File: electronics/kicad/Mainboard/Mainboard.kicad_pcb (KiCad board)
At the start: 2 copper layers, 99 x 53 mm, 32 parts, among them J1 MCU Power, J10 Box Button 1, J11 Box Button 2, J12 Conn_01x05, J13 Extra Button, J2 Conn_01x05, J3 Conn_01x05, J4 Conn_01x05, J5 Conn_01x05, J6 Conn_01x05, J7 X-Axis Hall, J8 Y-Axis Hall, J9 USB_A_Stacked, M2 MountingHole_2.7mm_M2.5_DIN96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, M2.5 MountingHole_2.7mm_M2.5_DIN96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, U1 ESP32-C6-DevKitC-1, U2 MCP23017_SP, U3 SP3485CP

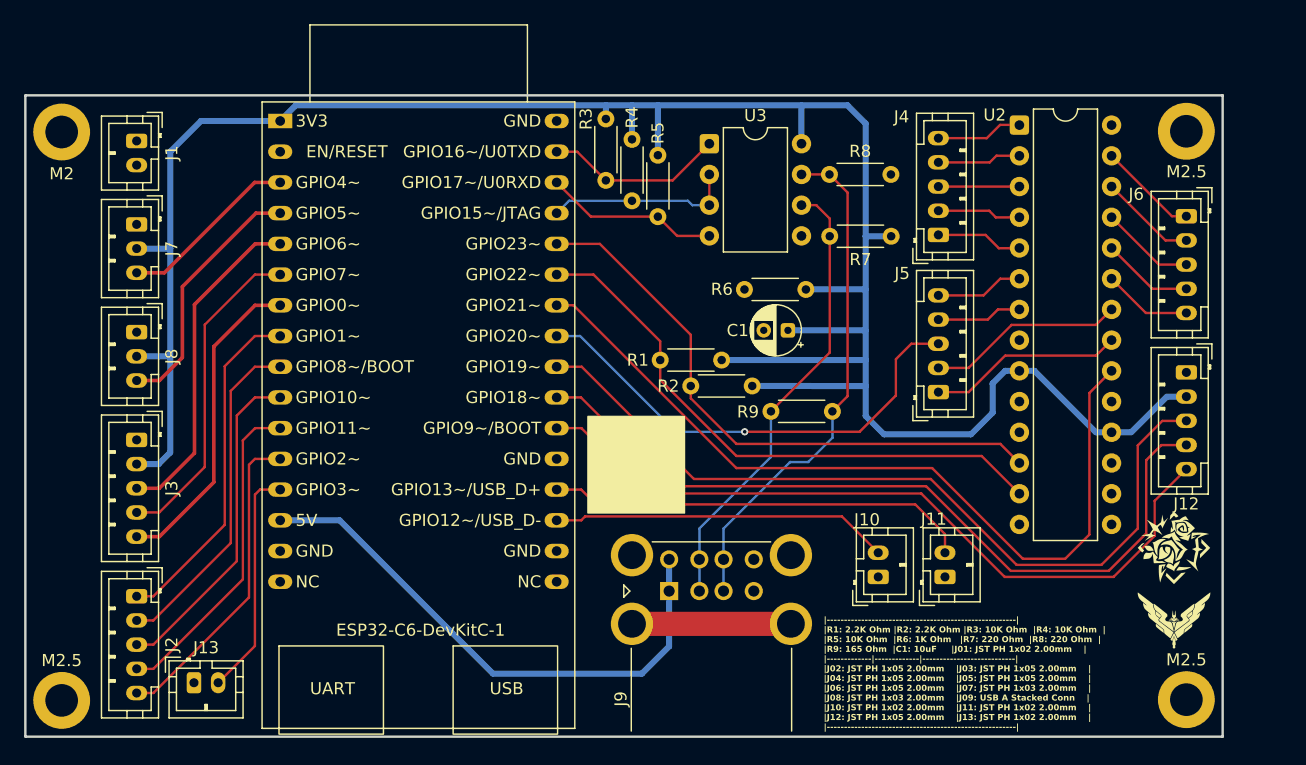
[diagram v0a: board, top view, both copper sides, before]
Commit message: Updated PCB with New Silkscreen
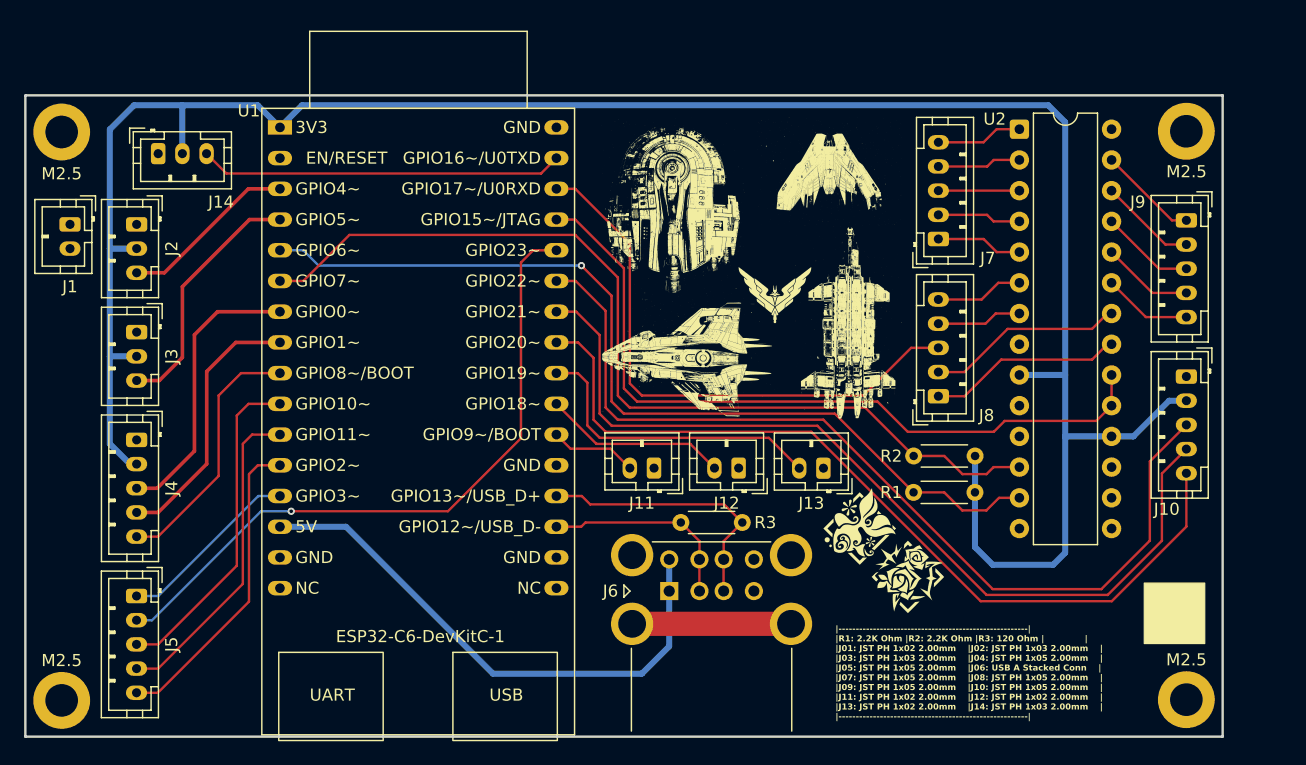
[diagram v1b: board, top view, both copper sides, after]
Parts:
- removed C1: 10uf, Capacitor_THT:CP_Radial_D4.0mm_P2.00mm
- removed R4, R5: 10K, Resistor_THT:R_Axial_DIN0204_L3.6mm_D1.6mm_P5.08mm_Horizontal
- removed R6: 1K, Resistor_THT:R_Axial_DIN0204_L3.6mm_D1.6mm_P5.08mm_Horizontal
- removed R7, R8: 220Ω, Resistor_THT:R_Axial_DIN0204_L3.6mm_D1.6mm_P5.08mm_Horizontal
- removed R9: 165Ω, Resistor_THT:R_Axial_DIN0204_L3.6mm_D1.6mm_P5.08mm_Horizontal
- removed U3: SP3485CP, Package_DIP:DIP-8_W7.62mm
- added G***: LOGO, Kicad Library:Cobra5, F.Cu at (167.5, 78.5)
- added G***: LOGO, Kicad Library:Carrier, F.Cu at (169.0, 91.0)
- added G***: LOGO, Kicad Library:Caspian, F.Cu at (154.5, 81.5)
- added G***: LOGO, Kicad Library:Python2, F.Cu at (156.0, 94.0)
- added G***: LOGO, Kicad Library:yoi-con, F.Cu at (170.0, 107.8)
- added J14: LED Strip, Connector_JST:JST_PH_B3B-PH-K_1x03_P2.00mm_Vertical, F.Cu at (112.0, 77.0)
- J1: value MCU Power -> GND Pair
- J10: value Box Button 1 -> Conn_01x05; footprint Connector_JST:JST_PH_B2B-PH-K_1x02_P2.00mm_Vertical -> Connector_JST:JST_PH_B5B-PH-K_1x05_P2.00mm_Vertical
- J11: value Box Button 2 -> Box Switch 1
- J12: value Conn_01x05 -> Box Switch 2; footprint Connector_JST:JST_PH_B5B-PH-K_1x05_P2.00mm_Vertical -> Connector_JST:JST_PH_B2B-PH-K_1x02_P2.00mm_Vertical
- J13: value Extra Button -> Bos Switch 3
- J2: value Conn_01x05 -> X-Axis Hall; footprint Connector_JST:JST_PH_B5B-PH-K_1x05_P2.00mm_Vertical -> Connector_JST:JST_PH_B3B-PH-K_1x03_P2.00mm_Vertical
- J3: value Conn_01x05 -> Y-Axis Hall; footprint Connector_JST:JST_PH_B5B-PH-K_1x05_P2.00mm_Vertical -> Connector_JST:JST_PH_B3B-PH-K_1x03_P2.00mm_Vertical
- J6: value Conn_01x05 -> USB_A_Stacked; footprint Connector_JST:JST_PH_B5B-PH-K_1x05_P2.00mm_Vertical -> Connector_USB:USB_A_CUI_UJ2-ADH-TH_Horizontal_Stacked
- J7: value X-Axis Hall -> Conn_01x05; footprint Connector_JST:JST_PH_B3B-PH-K_1x03_P2.00mm_Vertical -> Connector_JST:JST_PH_B5B-PH-K_1x05_P2.00mm_Vertical
- J8: value Y-Axis Hall -> Conn_01x05; footprint Connector_JST:JST_PH_B3B-PH-K_1x03_P2.00mm_Vertical -> Connector_JST:JST_PH_B5B-PH-K_1x05_P2.00mm_Vertical
- J9: value USB_A_Stacked -> Conn_01x05; footprint Connector_USB:USB_A_CUI_UJ2-ADH-TH_Horizontal_Stacked -> Connector_JST:JST_PH_B5B-PH-K_1x05_P2.00mm_Vertical
- R3: value 10K -> 120
- moved J4 68.4 mm to (110.2, 100.7), turned to -90 degrees
- moved J5 68.4 mm to (110.2, 113.6), turned to -90 degrees
- moved J8 66.5 mm to (176.5, 97.1), turned to 90 degrees
- moved J7 66.3 mm to (176.5, 84.1), turned to 90 degrees
- moved J13 55.0 mm to (167.0, 103.0), turned to 180 degrees
- moved J6 52.8 mm to (154.3, 113.2), turned to 90 degrees
- moved J9 52.6 mm to (197.0, 82.5), turned to -90 degrees
- moved G*** 42.6 mm to (163.0, 88.7)
- moved J12 37.9 mm to (160.0, 103.0), turned to 180 degrees
- moved R3 35.2 mm to (160.3, 107.5), turned to 180 degrees
- moved J2 30.8 mm to (110.2, 82.8)
- moved J10 30.4 mm to (197.0, 95.4), turned to -90 degrees
- moved J11 25.7 mm to (153.0, 103.0), turned to 180 degrees
- moved R1 23.6 mm to (179.5, 105.0)
- moved G*** 22.1 mm to (174.0, 112.0)
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- renumbered M2 to M2.5
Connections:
- J10 pad 2: Box Button 1 -> Vcc
- J11 pad 2: Box Button 2 -> Box Switch 1
- J12 pad 2: Vcc -> Box Switch 2
- J13 pad 2: Extra -> Box Switch 3
- J2 pad 1: Primary Trigger -> GND
- J2 pad 2: Secondary Trigger -> Vcc
- J2 pad 3: Base Button -> X-Axis
- J3 pad 3: Joystick X -> Y-Axis
- J4 pad 1: Face Hat Left - Up -> GND
- J4 pad 2: Face Hat Left - Right -> Vcc
- J4 pad 3: Face Hat Left - Down -> Joystick X
- J4 pad 4: Face Hat Left - Left -> Joystick Y
- J4 pad 5: Face Hat Left - Center -> Joystick Button
- J5 pad 1: Face Hat Right - Center -> Primary Trigger
- J5 pad 2: Face Hat Right - Left -> Secondary Trigger
- J5 pad 3: Face Hat Right - Down -> Base Button
- J5 pad 4: Face Hat Right - Right -> Head Button
- J5 pad 5: Face Hat Right - Up -> Face Button
- J6 pad 1: Thumb Hat - Left -> 5V
- J6 pad 2: Thumb Hat - Center -> CAN-LOW
- J6 pad 3: Thumb Hat - Up -> CAN-HI
- J6 pad 4: Thumb Hat - Right -> GND
- J6 pad 5: Thumb Hat - Down -> 5V
- J7 pad 1: GND -> Face Hat Left - Up
- J7 pad 2: Vcc -> Face Hat Left - Right
- J7 pad 3: X-Axis -> Face Hat Left - Down
- J8 pad 1: GND -> Face Hat Right - Center
- J8 pad 2: Vcc -> Face Hat Right - Left
- J8 pad 3: Y-Axis -> Face Hat Right - Down
- J9 pad 1: 5V -> Thumb Hat - Left
- J9 pad 2: RS485-A -> Thumb Hat - Center
- J9 pad 3: RS485-B -> Thumb Hat - Up
- J9 pad 4: GND -> Thumb Hat - Right
- J9 pad 5: 5V -> Thumb Hat - Down
- R1 pad 2: /SDA -> SDA
- R2 pad 2: /SCK -> SCK
- R3 pad 1: Vcc -> CAN-HI
- R3 pad 2: UART-TX -> CAN-LOW
- U1 pad 13: Extra -> Primary Trigger
- U1 pad 19: Box Button 1 -> CAN-LOW
- U1 pad 20: Box Button 2 -> CAN-HI
- U1 pad 22: RE B -> Box Switch 1
- U1 pad 23: RE A -> Box Switch 2
- U1 pad 24: RE Switch -> Box Switch 3
- U1 pad 25: Face Hat Right - Down -> RE B
- U1 pad 26: /INT A -> RE A
- U1 pad 27: /SDA -> RE Switch
- U1 pad 28: /SCK -> Secondary Trigger
- U1 pad 29: RDE -> INT
- U1 pad 30: UART-RX -> Face Hat Right - Down
- U1 pad 31: UART-TX -> Extra
- U1 pad 5: Joystick X -> SDA
- U1 pad 6: Joystick Button -> SCK
- U1 pad 7: Joystick Y -> Joystick X
- U1 pad 8: Primary Trigger -> Joystick Y
- U1 pad 9: Secondary Trigger -> Joystick Button
- U2 pad 12: /SCK -> SCK
- U2 pad 13: /SDA -> SDA
- U2 pad 19: unconnected-(U2-INTB-Pad19) -> INT
- U2 pad 20: /INT A -> INT
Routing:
- net SCK: track 0.00 -> 76.9 mm
- net SDA: track 0.00 -> 75.6 mm, vias 0 -> 1
- net /INT A: track 67.9 -> 0.00 mm
- net INT: track 0.00 -> 62.4 mm
- net /SCK: track 48.8 -> 0.00 mm
- net /SDA: track 47.6 -> 0.00 mm
- net RS485-B: track 42.5 -> 0.00 mm
- net RS485-A: track 38.1 -> 0.00 mm
- net Box Button 2: track 35.2 -> 0.00 mm
- net Secondary Trigger: track 27.9 -> 55.9 mm, vias 0 -> 1
- net Box Button 1: track 28.0 -> 0.00 mm
- net Box Switch 3: track 0.00 -> 25.4 mm
- net CAN-HI: track 0.00 -> 22.6 mm
- net CAN-LOW: track 0.00 -> 16.7 mm
- net RDE: track 15.7 -> 0.00 mm
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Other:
- board text added: "|-------------------------------------------------------| |R1: 2.2K Ohm |R2: 2.2K Ohm |R3: 120 Ohm | | |J01: JST PH 1x02 2.00mm |J02: JST PH 1x03 2.00mm | |J03: JST PH 1x03 2.00mm |J04: JST PH 1x05 2.00mm | |J05: JST PH 1x05 2.00mm |J06: USB A Stacked Conn | |J07: JST PH 1x05 2.00mm |J08: JST PH 1x05 2.00mm | |J09: JST PH 1x05 2.00mm |J10: JST PH 1x05 2.00mm | |J11: JST PH 1x02 2.00mm |J12: JST P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"
- board text removed: "|-------------------------------------------------------| |R1: 2.2K Ohm |R2: 2.2K Ohm |R3: 10K Ohm |R4: 10K Ohm | |R5: 10K Ohm |R6: 1K Ohm |R7: 220 Ohm |R8: 220 Ohm | |R9: 165 Ohm |C1: 10uF |J01: JST PH 1x02 2.00mm | |-------------|-------------|---------------------------| |J02: JST PH 1x05 2.00mm |J03: JST PH 1x05 2.00mm | |J04: JST PH 1x05 2.00mm |J05: JST PH 1x05 2.00mm | |J06: JST PH 1x05 2.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"
